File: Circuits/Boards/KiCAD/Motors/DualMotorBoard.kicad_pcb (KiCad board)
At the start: 2 copper layers, 127 x 101.6 mm, 114 parts, among them J1 Conn_01x05, J10 Conn_01x01, J11 Conn_01x01, J12 Conn_01x01, J13 Conn_01x01, J14 Conn_01x01, J15 Conn_01x02, J16 Conn_01x02, J17 MC34063, J2 Conn_01x01, J3 Conn_01x01, J4 Conn_01x01, J5 Conn_01x01, J6 Conn_01x01, J7 Conn_01x01, J8 Conn_01x05, J9 Conn_01x01, Q1 2N3904, Q10 Q_NMOS_DGS, Q11 Q_NMOS_DGS, Q12 Q_NMOS_DGS, Q13 Q_NMOS_DGS, Q14 2N3904, Q15 2N3904, Q16 2N3904, Q17 2N3904, Q18 2N3904, Q19 2N3904, Q2 2N3904, Q20 2N3904, Q21 2N3904, Q22 2N3904, Q23 Q_NMOS_DGS, Q24 Q_NMOS_DGS, Q25 Q_NMOS_DGS, Q26 Q_NMOS_DGS, Q3 2N3904, Q4 2N3904, Q5 2N3904, Q6 2N3904, Q7 2N3904, Q8 2N3904, Q9 2N3904, U2 LM7805_TO220

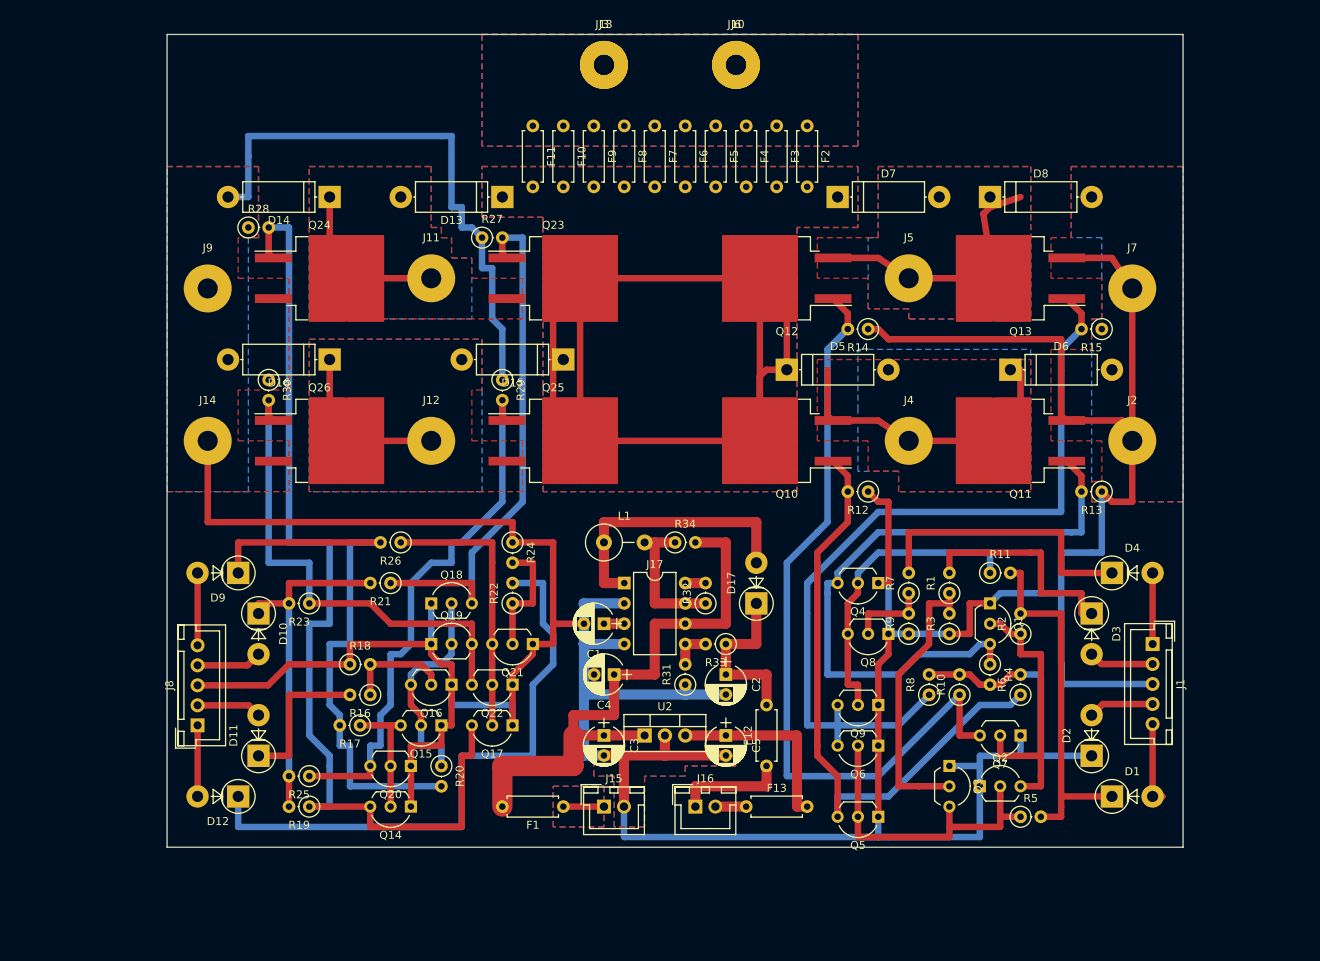
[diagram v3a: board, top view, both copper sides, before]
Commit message: Added drain resistors to gates
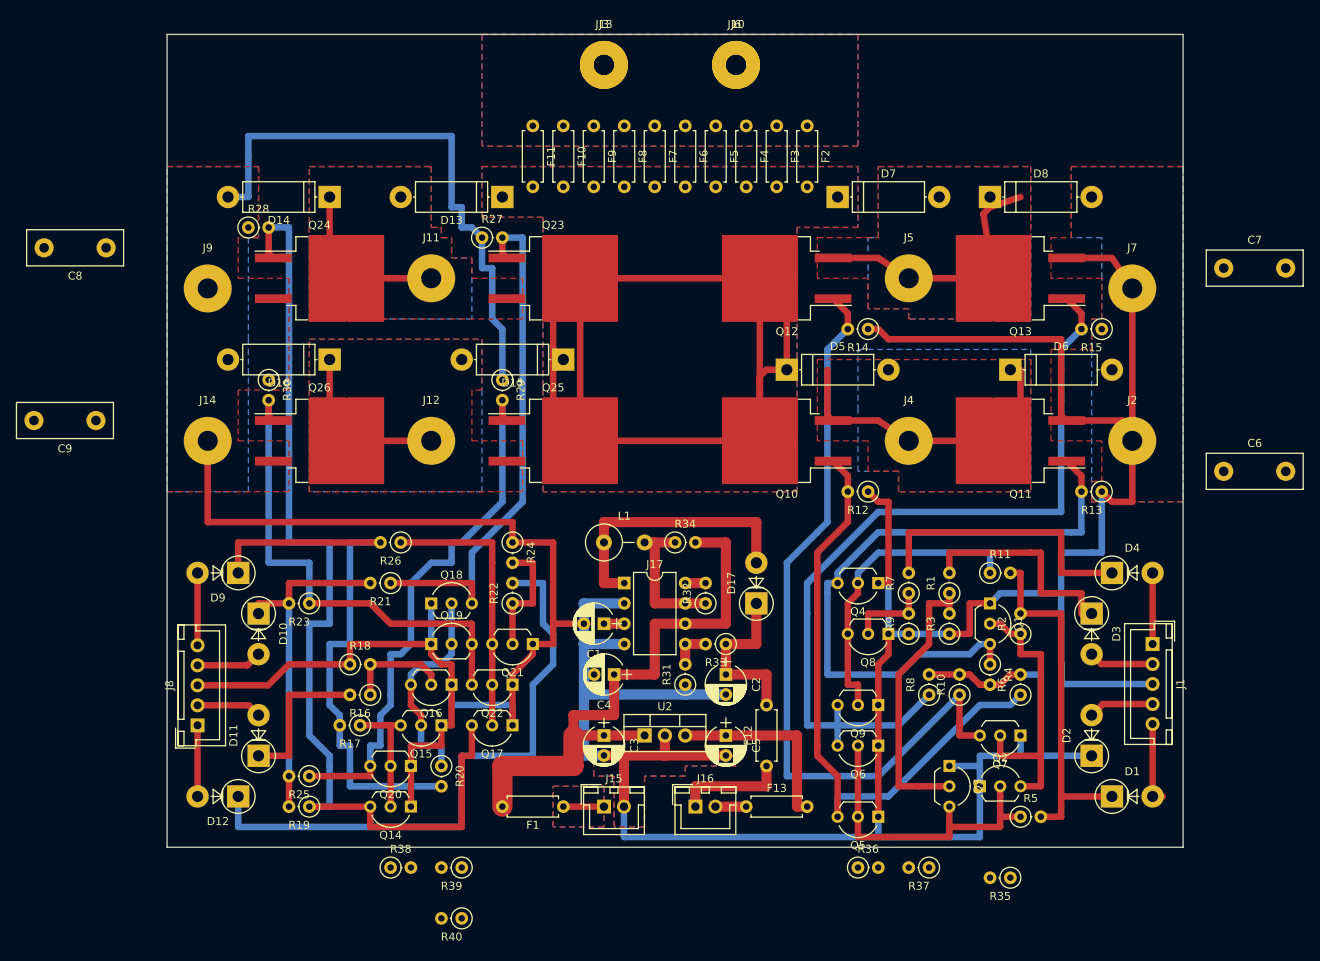
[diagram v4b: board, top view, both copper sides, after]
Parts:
- added C6: 1200uF, Capacitors_THT:C_Disc_D12.0mm_W4.4mm_P7.75mm, F.Cu at (259.1, 80.0)
- added C7: 1200uF, Capacitors_THT:C_Disc_D12.0mm_W4.4mm_P7.75mm, F.Cu at (259.1, 54.6)
- added C8: 1200uF, Capacitors_THT:C_Disc_D12.0mm_W4.4mm_P7.75mm, F.Cu at (119.4, 52.1)
- added C9: 1200uF, Capacitors_THT:C_Disc_D12.0mm_W4.4mm_P7.75mm, F.Cu at (118.1, 73.7)
- added R35: 10K, Resistors_THT:R_Axial_DIN0207_L6.3mm_D2.5mm_P2.54mm_Vertical, F.Cu at (232.4, 130.8)
- added R36: 10K, Resistors_THT:R_Axial_DIN0207_L6.3mm_D2.5mm_P2.54mm_Vertical, F.Cu at (213.4, 129.5)
- added R37: 10K, Resistors_THT:R_Axial_DIN0207_L6.3mm_D2.5mm_P2.54mm_Vertical, F.Cu at (222.2, 129.5)
- added R38: 10K, Resistors_THT:R_Axial_DIN0207_L6.3mm_D2.5mm_P2.54mm_Vertical, F.Cu at (154.9, 129.5)
- added R39: 10K, Resistors_THT:R_Axial_DIN0207_L6.3mm_D2.5mm_P2.54mm_Vertical, F.Cu at (163.8, 129.5)
- added R40: 10K, Resistors_THT:R_Axial_DIN0207_L6.3mm_D2.5mm_P2.54mm_Vertical, F.Cu at (163.8, 135.9)

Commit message: Motor HF adjustments (gate drain resistors)
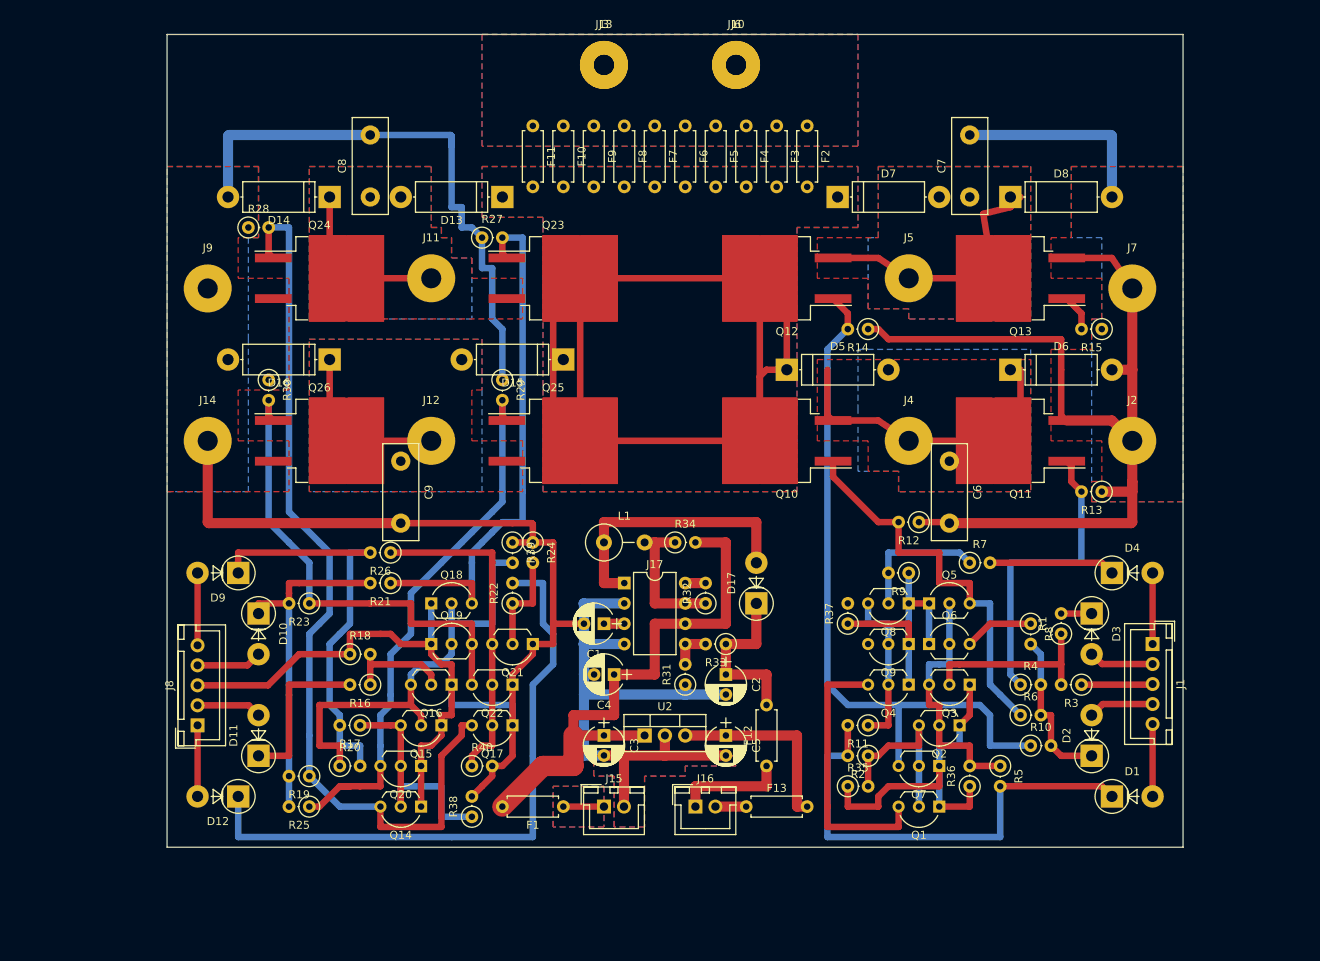
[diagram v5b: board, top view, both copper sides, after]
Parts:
- moved R39 41.1 mm to (170.2, 88.9), turned to 270 degrees
- moved C9 38.4 mm to (156.2, 78.7), turned to 270 degrees
- moved C6 34.3 mm to (224.8, 78.7), turned to 270 degrees
- moved C8 33.6 mm to (152.4, 45.7), turned to 90 degrees
- moved C7 33.0 mm to (227.3, 45.7), turned to 90 degrees
- moved R37 32.1 mm to (212.1, 99.1), turned to 90 degrees
- moved Q5 27.4 mm to (222.2, 96.5), turned to 0 degrees
- moved Q1 26.2 mm to (223.5, 121.9), turned to 180 degrees
- moved R11 24.4 mm to (214.6, 111.8), turned to 180 degrees
- moved R2 24.4 mm to (214.6, 115.6), turned to 180 degrees
- moved R35 23.3 mm to (212.1, 119.4), turned to 0 degrees
- moved R40 19.1 mm to (165.1, 116.8), turned to 0 degrees
- moved R3 17.7 mm to (241.3, 106.7), turned to 180 degrees
- moved R36 17.3 mm to (227.3, 119.4), turned to 90 degrees
- moved R8 15.5 mm to (234.9, 99.1), turned to 270 degrees
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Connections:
- R35 pad 1: /MotorControlUnit_1/MBB -> GND
- R35 pad 2: GND -> /MotorControlUnit_1/MBB
- R36 pad 1: /MotorControlUnit_1/MFB -> GND
- R36 pad 2: GND -> /MotorControlUnit_1/MFB
- R37 pad 1: /MotorControlUnit_1/iSpeed -> GND
- R37 pad 2: GND -> /MotorControlUnit_1/iSpeed
- R38 pad 1: /MotorControlUnit_2/MBB -> GND
- R38 pad 2: GND -> /MotorControlUnit_2/MBB
- R39 pad 1: /MotorControlUnit_2/MFB -> GND
- R39 pad 2: GND -> /MotorControlUnit_2/MFB
- R40 pad 1: /MotorControlUnit_2/iSpeed -> GND
- R40 pad 2: GND -> /MotorControlUnit_2/iSpeed
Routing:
- net /MotorControlUnit_1/FBM: track 105.4 -> 13.2 mm
- net /MotorControlUnit_2/MFB: track 27.0 -> 56.2 mm
- net /MotorControlUnit_1/MFF: track 78.5 -> 50.2 mm
- net /MotorControlUnit_1/Dir: track 27.9 -> 3.81 mm
- net GND: track 586.6 -> 563.2 mm
- net /MotorControlUnit_1/Speed: track 35.6 -> 15.8 mm
- net /MotorControlUnit_2/DVSW: track 71.6 -> 52.4 mm
- net /MotorControlUnit_1/iSpeed: track 38.4 -> 20.3 mm
- net /MotorControlUnit_1/DVSW: track 45.7 -> 58.9 mm
- net /MotorControlUnit_1/DirSel: track 35.9 -> 22.9 mm
- net /MotorControlUnit_1/MBB: track 36.1 -> 23.4 mm
- net /MotorControlUnit_2/BBM: track 125.8 -> 114.0 mm
- net /MotorControlUnit_1/DVG: track 31.5 -> 20.1 mm
- net /MotorControlUnit_1/MFB: track 40.6 -> 31.7 mm
- net /MotorControlUnit_1/MBF: track 97.0 -> 88.5 mm
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
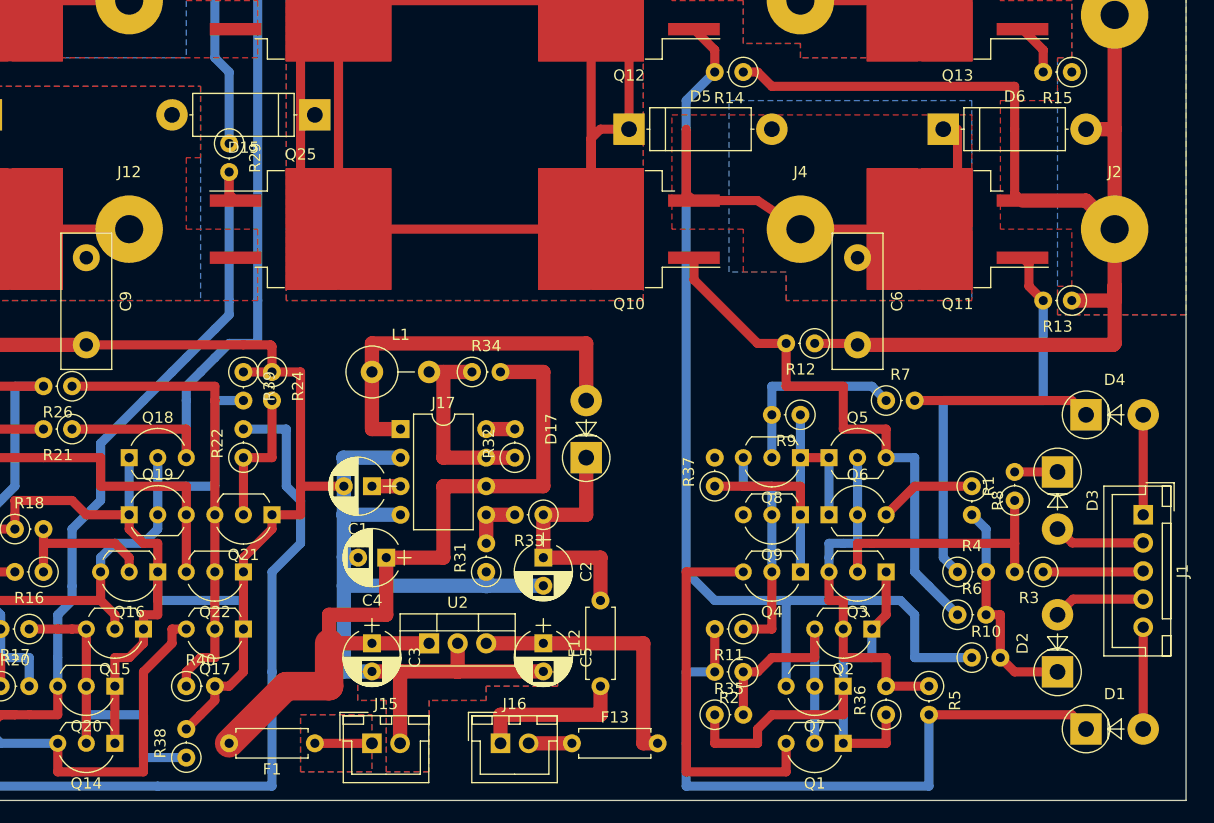
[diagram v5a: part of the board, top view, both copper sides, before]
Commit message: Finished rerouting board with new resistors and caps
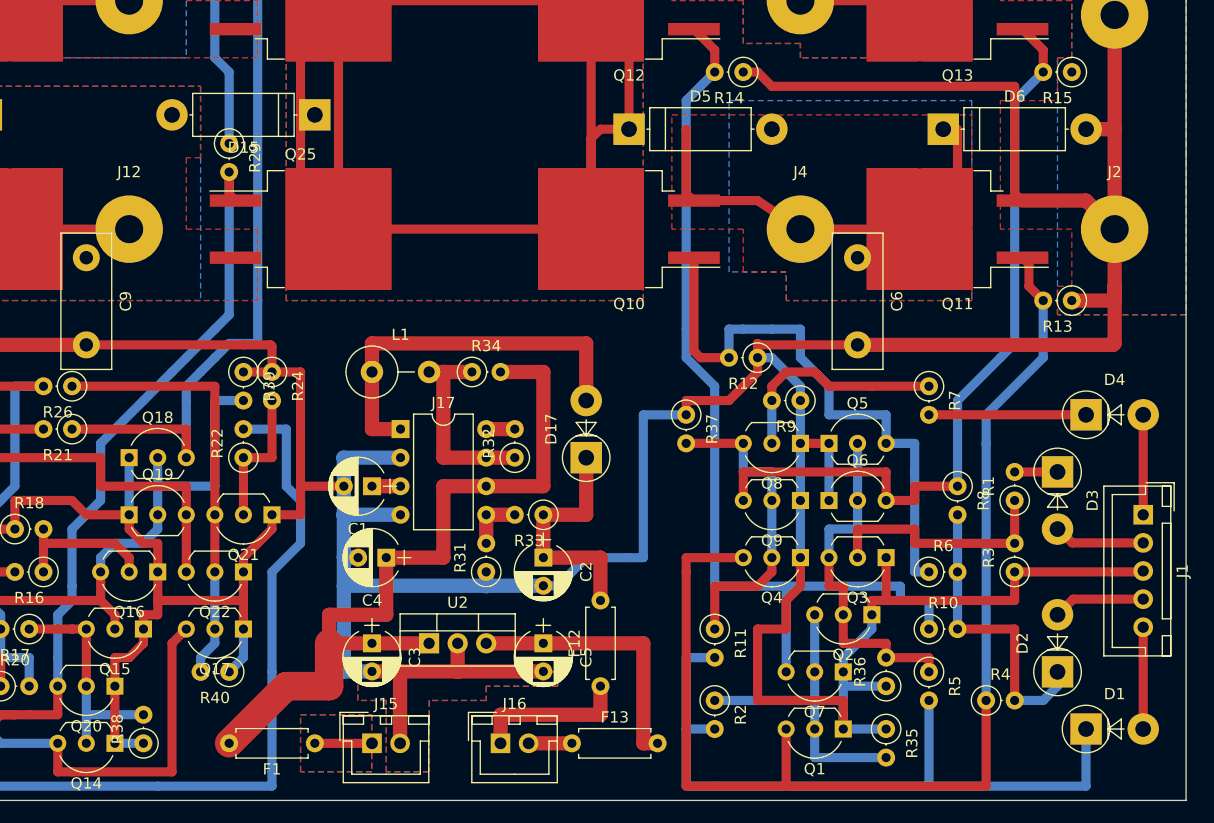
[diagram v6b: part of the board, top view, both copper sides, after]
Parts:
- moved R35 15.3 mm to (227.3, 120.7), turned to 270 degrees
- moved R4 11.7 mm to (236.2, 118.1)
- moved R37 6.84 mm to (209.6, 92.7), turned to 270 degrees
- moved R12 5.24 mm to (215.9, 87.6)
- moved R6 4.58 mm to (231.1, 106.7)
- moved R10 4.58 mm to (231.1, 111.8)
- moved R40 4.02 mm to (168.9, 115.6), turned to 180 degrees
- moved R38 4.02 mm to (161.3, 121.9)
- moved R7 4.02 mm to (231.1, 90.2), turned to 270 degrees
- moved R2 3.59 mm to (212.1, 118.1), turned to 270 degrees
- moved R3 2.54 mm to (238.8, 106.7), turned to 90 degrees
- moved R11 2.54 mm to (212.1, 111.8), turned to 270 degrees
- moved R36 2.54 mm to (227.3, 116.8)
- moved Q2 1.27 mm to (226.1, 110.5)
- moved Q3 1.27 mm to (227.3, 105.4)
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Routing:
- net /MotorControlUnit_1/FBM: track 13.2 -> 70.0 mm
- net GND: track 563.2 -> 605.9 mm
- net /MotorControlUnit_1/BBM: track 72.4 -> 107.0 mm
- net /MotorControlUnit_1/iSpeed: track 20.3 -> 28.5 mm
- net /MotorControlUnit_1/DVG: track 20.1 -> 27.2 mm
- net /MotorControlUnit_1/DVSW: track 58.9 -> 64.8 mm
- net /MotorControlUnit_1/MBF: track 88.5 -> 82.9 mm
- net /MotorControlUnit_1/MBB: track 23.4 -> 27.9 mm
- net /MotorControlUnit_1/SpeedSel: track 17.0 -> 20.1 mm
- net /MotorControlUnit_1/MFF: track 50.2 -> 52.7 mm
- net /MotorControlUnit_1/Speed: track 15.8 -> 14.0 mm
- net /MotorControlUnit_1/DirSel: track 22.9 -> 21.6 mm
- net /MotorControlUnit_2/MBB: track 21.4 -> 20.3 mm
- net /MotorControlUnit_2/iSpeed: track 39.4 -> 38.6 mm
- net /MotorControlUnit_2/BBM: track 114.0 -> 114.7 mm
